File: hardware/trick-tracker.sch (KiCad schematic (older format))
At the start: 56 parts, among them J1 USB4105-GF-A, J2 S2B-PH-K, J3 QWiiC, J4 MEM2061-01-188-00-A, J5 Conn_01x08_Male, J6 QWiiC, P1 SMTB-1240-S-R, U1 MS88SF2, U2 DPS368XTSA1, U4 MCP73831/OT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

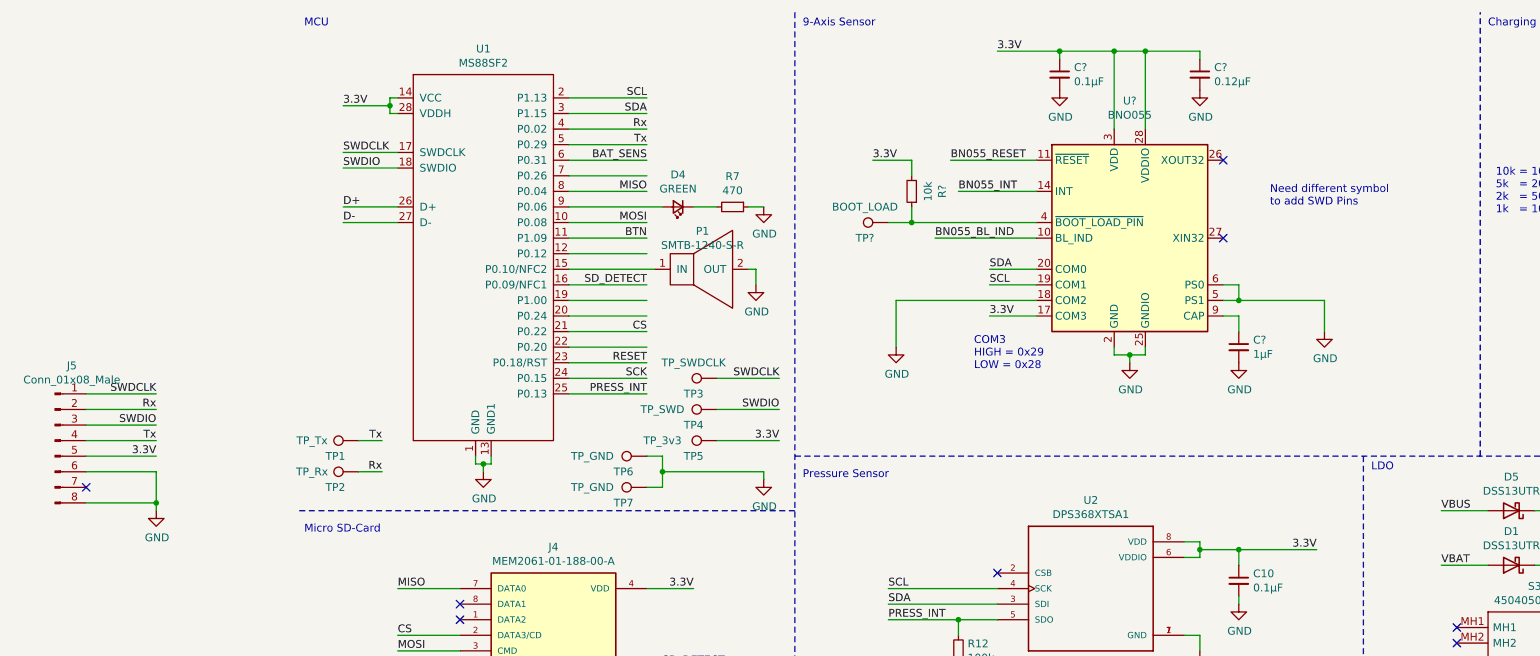
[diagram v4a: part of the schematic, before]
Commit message: Add and layed out BMX160 Sensor
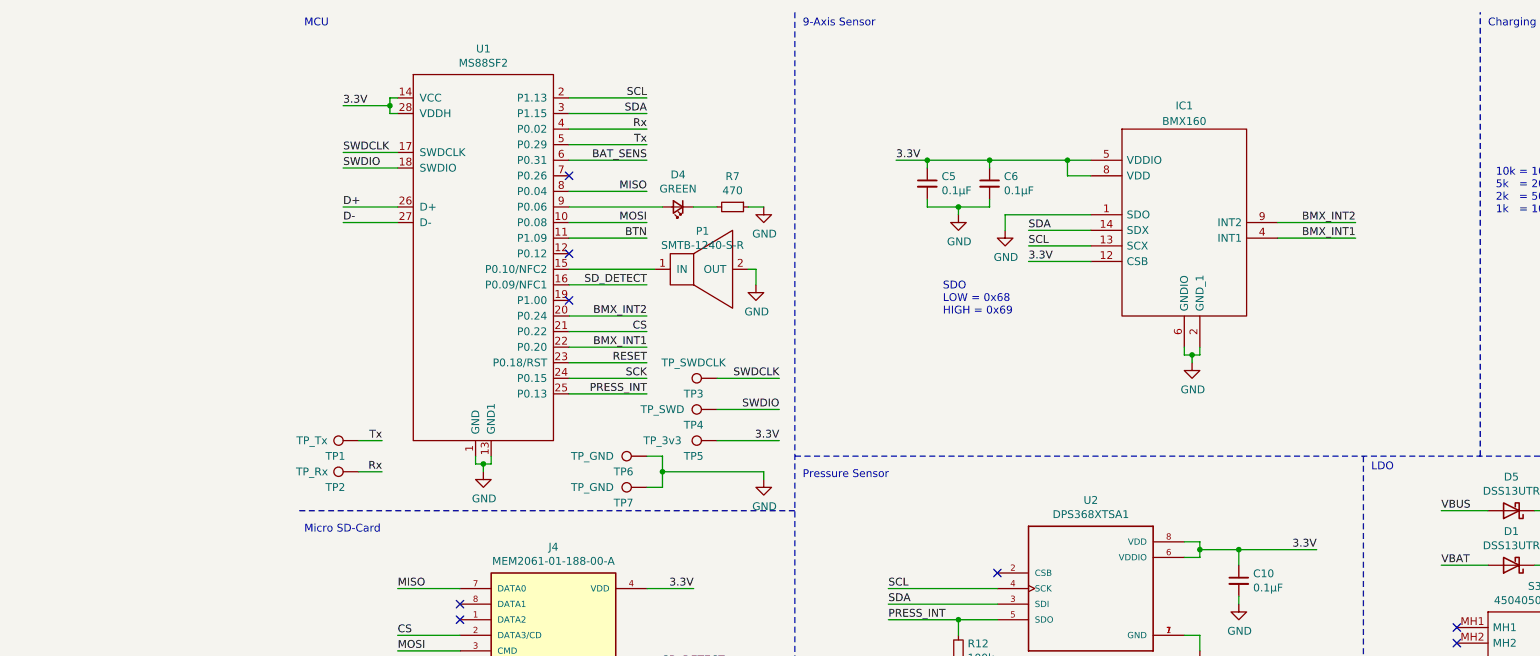
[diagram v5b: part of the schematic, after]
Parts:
- removed C?: 0.12µF, Capacitor_SMD:C_0603_1608Metric, symbol Device:C_Small
- removed C?: 0.1µF, Capacitor_SMD:C_0603_1608Metric, symbol Device:C_Small
- removed C?: 1µF, Capacitor_SMD:C_0603_1608Metric, symbol Device:C_Small
- removed J5: Conn_01x08_Male, Connector_PinSocket_2.54mm:PinSocket_2x04_P2.54mm_Vertical_SMD, symbol Connector:Conn_01x08_Male
- removed R?: 10k, Resistor_SMD:R_0603_1608Metric, symbol Device:R_Small
- removed TP?: BOOT_LOAD, TestPoint:TestPoint_Pad_D1.5mm, symbol Connector:TestPoint
- removed U?: BNO055, Package_LGA:LGA-28_5.2x3.8mm_P0.5mm, symbol Sensor_Motion:BNO055
- added C5, C6: 0.1µF, Capacitor_SMD:C_0603_1608Metric, symbol Device:C_Small
- added IC1: BMX160, BMX160:PQFN50P300X250X88-14N, symbol BMX160:BMX160
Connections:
- net 3.3V: now also C5.1, C6.1, IC1.12 (CSB), IC1.5 (VDDIO), IC1.8 (VDD)
- net GND: now also C5.2, C6.2, IC1.1 (SDO), IC1.2 (GND_1), IC1.3 (GND_2), IC1.6 (GNDIO), IC1.7 (GND_3)
- net SCL: now also IC1.13 (SCX)
- net SDA: now also IC1.14 (SDX)
- net BMX_INT2: now reaches U1.20 (P0.24)
- net BMX_INT2: now also IC1.9 (INT2)
- net BMX_INT1: now reaches U1.22 (P0.20)
- net BMX_INT1: now also IC1.4 (INT1)
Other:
- note added: "SDO\nLOW = 0x68\nHIGH = 0x69"
- note removed: "COM3\nHIGH = 0x29\nLOW = 0x28"
- note removed: "Need different symbol\nto add SWD Pins"
